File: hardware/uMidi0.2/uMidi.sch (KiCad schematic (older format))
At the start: 6 parts, among them CON1 USB-MINI-B, IC1 ATXMEGA128A4U-M, IC2 6N136, P1 PDI, U1 74LS14

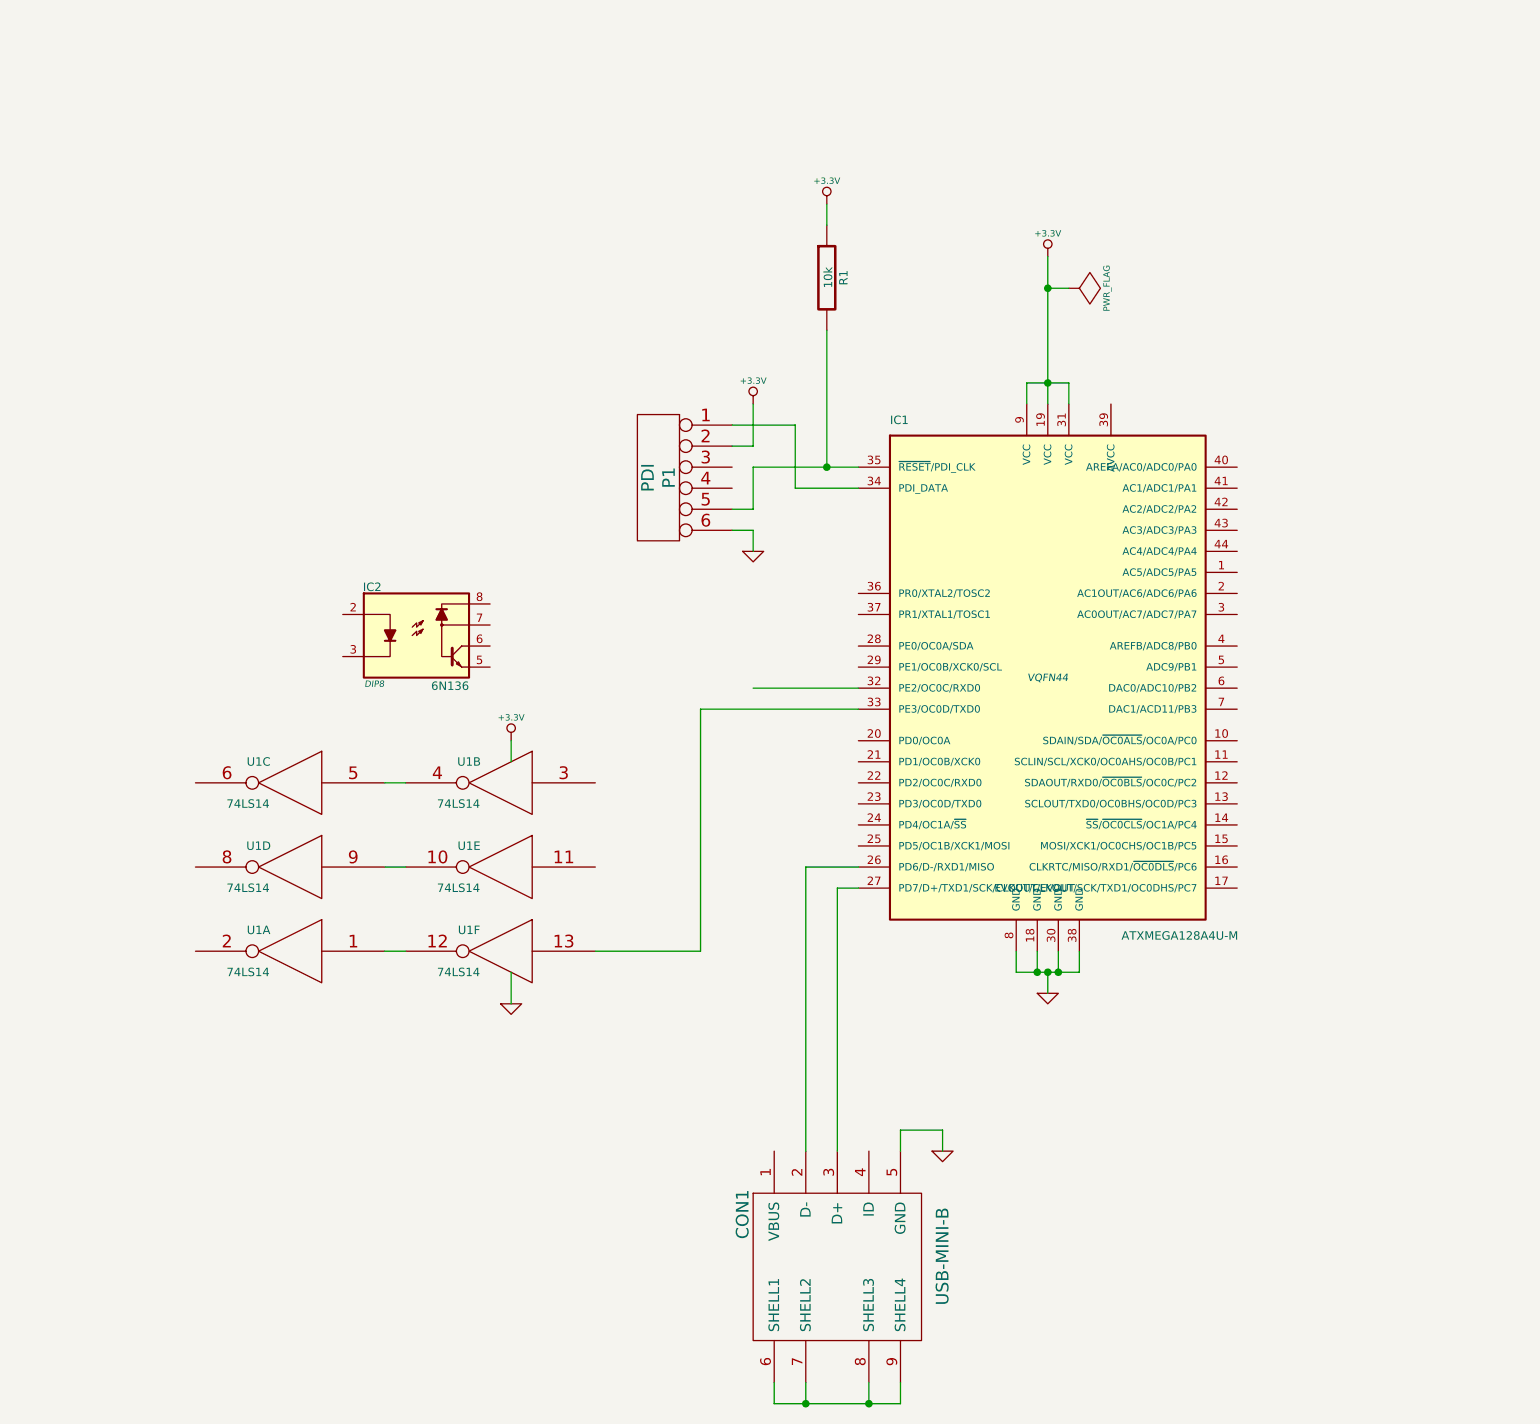
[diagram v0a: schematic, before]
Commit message: Add and connect midi output connectors
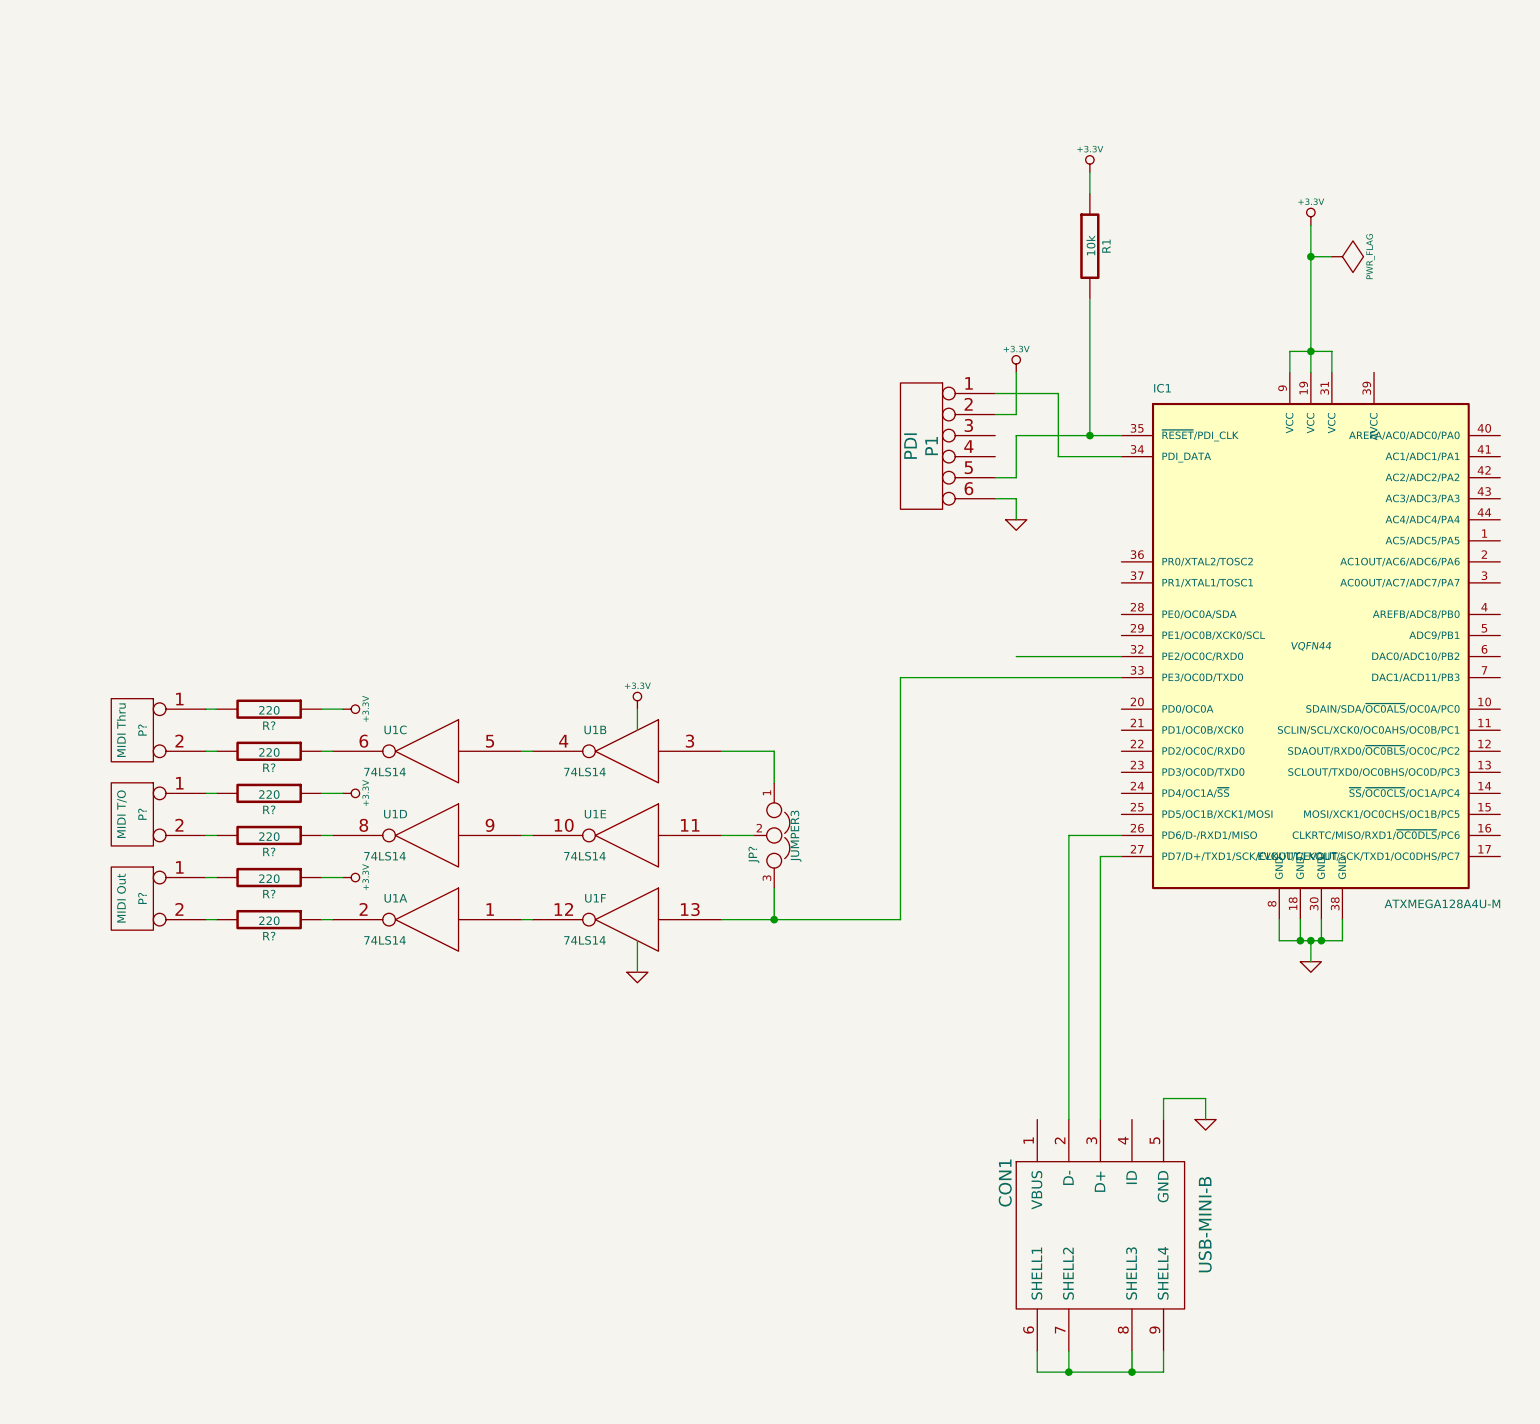
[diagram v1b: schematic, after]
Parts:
- removed IC2: 6N136, DIP8, symbol 6N136
- added JP?: JUMPER3, symbol JUMPER3
- added P?: MIDI Out, symbol CONN_2
- added P?: MIDI Thru, symbol CONN_2
- added P?: MIDI T/O, symbol CONN_2
- added R? (x6): 220, symbol R
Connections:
- net +3.3V: now also R?.1, R?.1, R?.1
- net at IC1.33 (PE3/OC0D/TXD0), U1.13: now also JP?.3
- net at U1.3: now also JP?.1
- net at U1.6: now also R?.1
- net at U1.8: now also R?.1
- net at U1.11: now also JP?.2
- net at U1.2: now also R?.1
- new net: P?.2 (PM), R?.2 (x3)
- new net: P?.1 (P1), R?.2 (x3)
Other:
- moved on the sheet: CON1, IC1, P1, R1, U1A, U1B, U1C, U1D, U1E, U1F

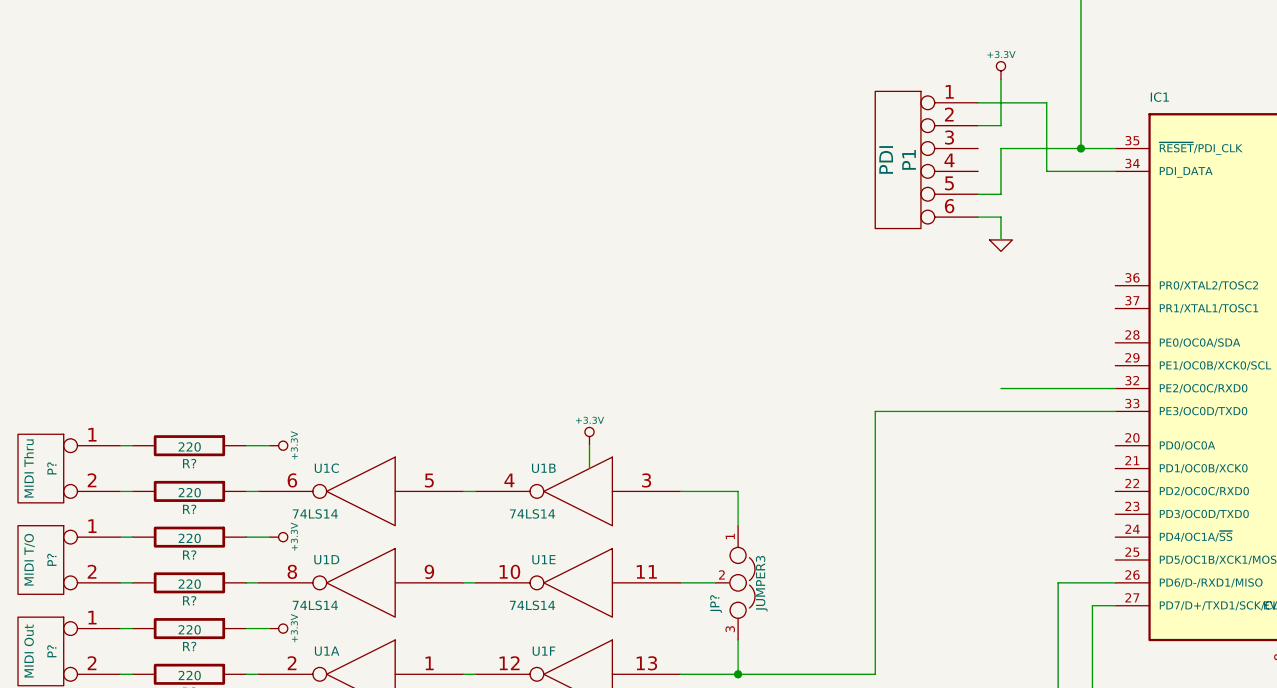
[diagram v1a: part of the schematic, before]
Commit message: Add midi input circuitry
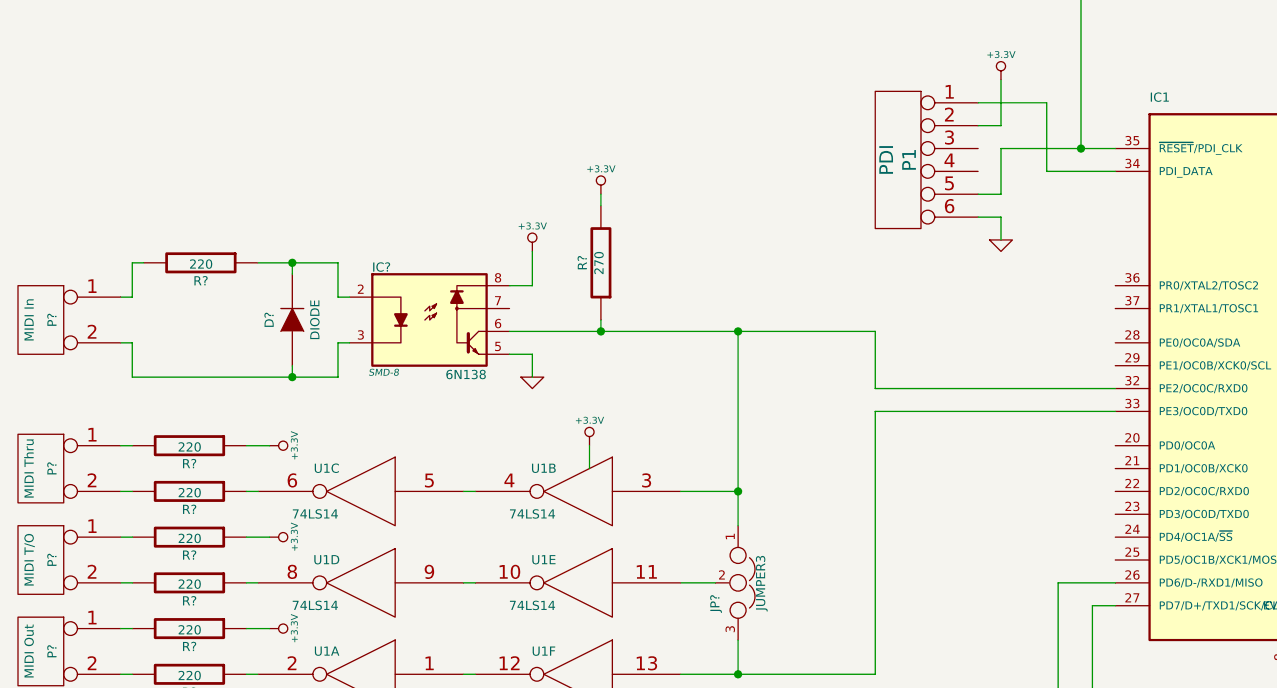
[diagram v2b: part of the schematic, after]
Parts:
- added D?: DIODE, symbol DIODE
- added IC?: 6N138, SMD-8, symbol 6N135
- added P?: MIDI In, symbol CONN_2
- added R?: 220, symbol R
- added R?: 270, symbol R
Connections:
- net +3.3V: now also IC?.8, R?.2
- net GND: now also IC?.5
- net at IC1.32 (PE2/OC0C/RXD0): now also JP?.1, U1.3, IC?.6, R?.1
- new net: P?.1 (P1), R?.2
- new net: D?.1 (A), IC?.3, P?.2 (PM)
- new net: D?.2 (K), IC?.2, R?.1
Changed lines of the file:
@@
 	5250 3900 6300 3900
 Wire Wire Line
-	6300 3800 5800 3800
+	5250 3800 6300 3800
 Wire Wire Line
 	3450 4250 3500 4250
@@
 Connection ~ 4650 5050
 Wire Wire Line
-	4650 4400 4650 4250
+	4650 3550 4650 4250
+Wire Wire Line
+	4650 4250 4650 4400
 Wire Wire Line
 	4650 4250 4400 4250
@@
 	-1   0    0    -1
 $EndComp
+$Comp
+L 6N135 IC?
+U 1 1 53C94FAA
+P 3300 3500
+F 0 "IC?" H 3090 3730 40  0000 C CNN
+F 1 "6N138" H 3460 3260 40  0000 C CNN
+F 2 "SMD-8" H 3100 3270 30  0000 C CIN
+F 3 "" H 3300 3500 60  0000 C CNN
+	1    3300 3500
+	1    0    0    -1
+$EndComp
+$Comp
+L R R?
+U 1 1 53C94FCB
+P 2300 3250
+F 0 "R?" V 2380 3250 40  0000 C CNN
+F 1 "220" V 2307 3251 40  0000 C CNN
+F 2 "" V 2230 3250 30  0000 C CNN
+F 3 "" H 2300 3250 30  0000 C CNN
+	1    2300 3250
+	0    1    1    0
+$EndComp
+$Comp
+L DIODE D?
+U 1 1 53C950D4
+P 2700 3500
+F 0 "D?" H 2700 3600 40  0000 C CNN
+F 1 "DIODE" H 2700 3400 40  0000 C CNN
+F 2 "" H 2700 3500 60  0000 C CNN
+F 3 "" H 2700 3500 60  0000 C CNN
+	1    2700 3500
+	0    -1   -1   0
+$EndComp
+Wire Wire Line
+	2000 3750 2700 3750
+Wire Wire Line
+	2700 3750 2900 3750
+Wire Wire Line
+	2900 3750 2900 3600
+Wire Wire Line
+	2900 3600 2950 3600
+Wire Wire Line
+	2700 3750 2700 3700
+Wire Wire Line
+	2000 3750 2000 3600
+Wire Wire Line
+	2000 3600 1950 3600
+Connection ~ 2700 3750
+Wire Wire Line
+	2550 3250 2700 3250
+Wire Wire Line
+	2700 3250 2900 3250
+Wire Wire Line
+	2900 3250 2900 3400
+Wire Wire Line
+	2900 3400 2950 3400
+Wire Wire Line
+	2700 3250 2700 3300
+Connection ~ 2700 3250
+$Comp
+L CONN_2 P?
+U 1 1 53C94EC8
+P 1600 3500
+F 0 "P?" V 1550 3500 40  0000 C CNN
+F 1 "MIDI In" V 1650 3500 40  0000 C CNN
+F 2 "" H 1600 3500 60  0000 C CNN
+F 3 "" H 1600 3500 60  0000 C CNN
+	1    1600 3500
+	-1   0    0    -1
+$EndComp
+Wire Wire Line
+	1950 3400 2000 3400
+Wire Wire Line
+	2000 3400 2000 3250
+Wire Wire Line
+	2000 3250 2050 3250
+$Comp
+L +3.3V #PWR?
+U 1 1 53C95524
+P 3750 3200
+F 0 "#PWR?" H 3750 3160 30  0001 C CNN
+F 1 "+3.3V" H 3750 3310 30  0000 C CNN
+F 2 "" H 3750 3200 60  0000 C CNN
+F 3 "" H 3750 3200 60  0000 C CNN
+	1    3750 3200
+	1    0    0    -1
+$EndComp
+$Comp
+L R R?
+U 1 1 53C9552F
+P 4050 3250
+F 0 "R?" V 4130 3250 40  0000 C CNN
+F 1 "270" V 4057 3251 40  0000 C CNN
+F 2 "" V 3980 3250 30  0000 C CNN
+F 3 "" H 4050 3250 30  0000 C CNN
+	1    4050 3250
+	-1   0    0    1
+$EndComp
+Wire Wire Line
+	3650 3350 3750 3350
+Wire Wire Line
+	3750 3350 3750 3200
+$Comp
+L +3.3V #PWR?
+U 1 1 53C956B4
+P 4050 2950
+F 0 "#PWR?" H 4050 2910 30  0001 C CNN
+F 1 "+3.3V" H 4050 3060 30  0000 C CNN
+F 2 "" H 4050 2950 60  0000 C CNN
+F 3 "" H 4050 2950 60  0000 C CNN
+	1    4050 2950
+	1    0    0    -1
+$EndComp
+Wire Wire Line
+	3650 3550 4050 3550
+Wire Wire Line
+	4050 3550 4650 3550
+Wire Wire Line
+	4650 3550 5250 3550
+Wire Wire Line
+	4050 3550 4050 3500
+Wire Wire Line
+	4050 3000 4050 2950
+$Comp
+L GND #PWR?
+U 1 1 53C9577E
+P 3750 3750
+F 0 "#PWR?" H 3750 3750 30  0001 C CNN
+F 1 "GND" H 3750 3680 30  0001 C CNN
+F 2 "" H 3750 3750 60  0000 C CNN
+F 3 "" H 3750 3750 60  0000 C CNN
+	1    3750 3750
+	1    0    0    -1
+$EndComp
+Wire Wire Line
+	3750 3750 3750 3650
+Wire Wire Line
+	3750 3650 3650 3650
+Wire Wire Line
+	5250 3550 5250 3800
+Connection ~ 4050 3550
+Connection ~ 4650 3550
+Connection ~ 4650 4250
 $EndSCHEMATC
